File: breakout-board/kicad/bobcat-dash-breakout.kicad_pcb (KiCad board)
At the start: 2 copper layers, 162 x 159 mm, 184 parts, among them J1 TO PI (40-pin ribbon), J10 ADS1115 PWR/I2C, J11 LIGHTS, J12 COIL, J13 TILT, J14 TEMP PROBE, J15 ADS1115 INPUTS, J16 MAX98357A STEREO, J17 POD, J2 POWER IN, J3 TO 5V BUCK, J4 SWITCHES, J5 TACH, J6 FUEL, J7 HORN, J8 SILENCE, J9 MAX98357A MONO, Q1 IRLZ44N, Q2 IRF4905, Q3 BC547B, Q4 BC547B, Q5 IRLZ44N, U1 PC817, U10 PC817, U11 DS18B20, U4 PC817, U5 PC817, U6 CD4060BE, U7 PC817, U8 PC817, U9 PC817

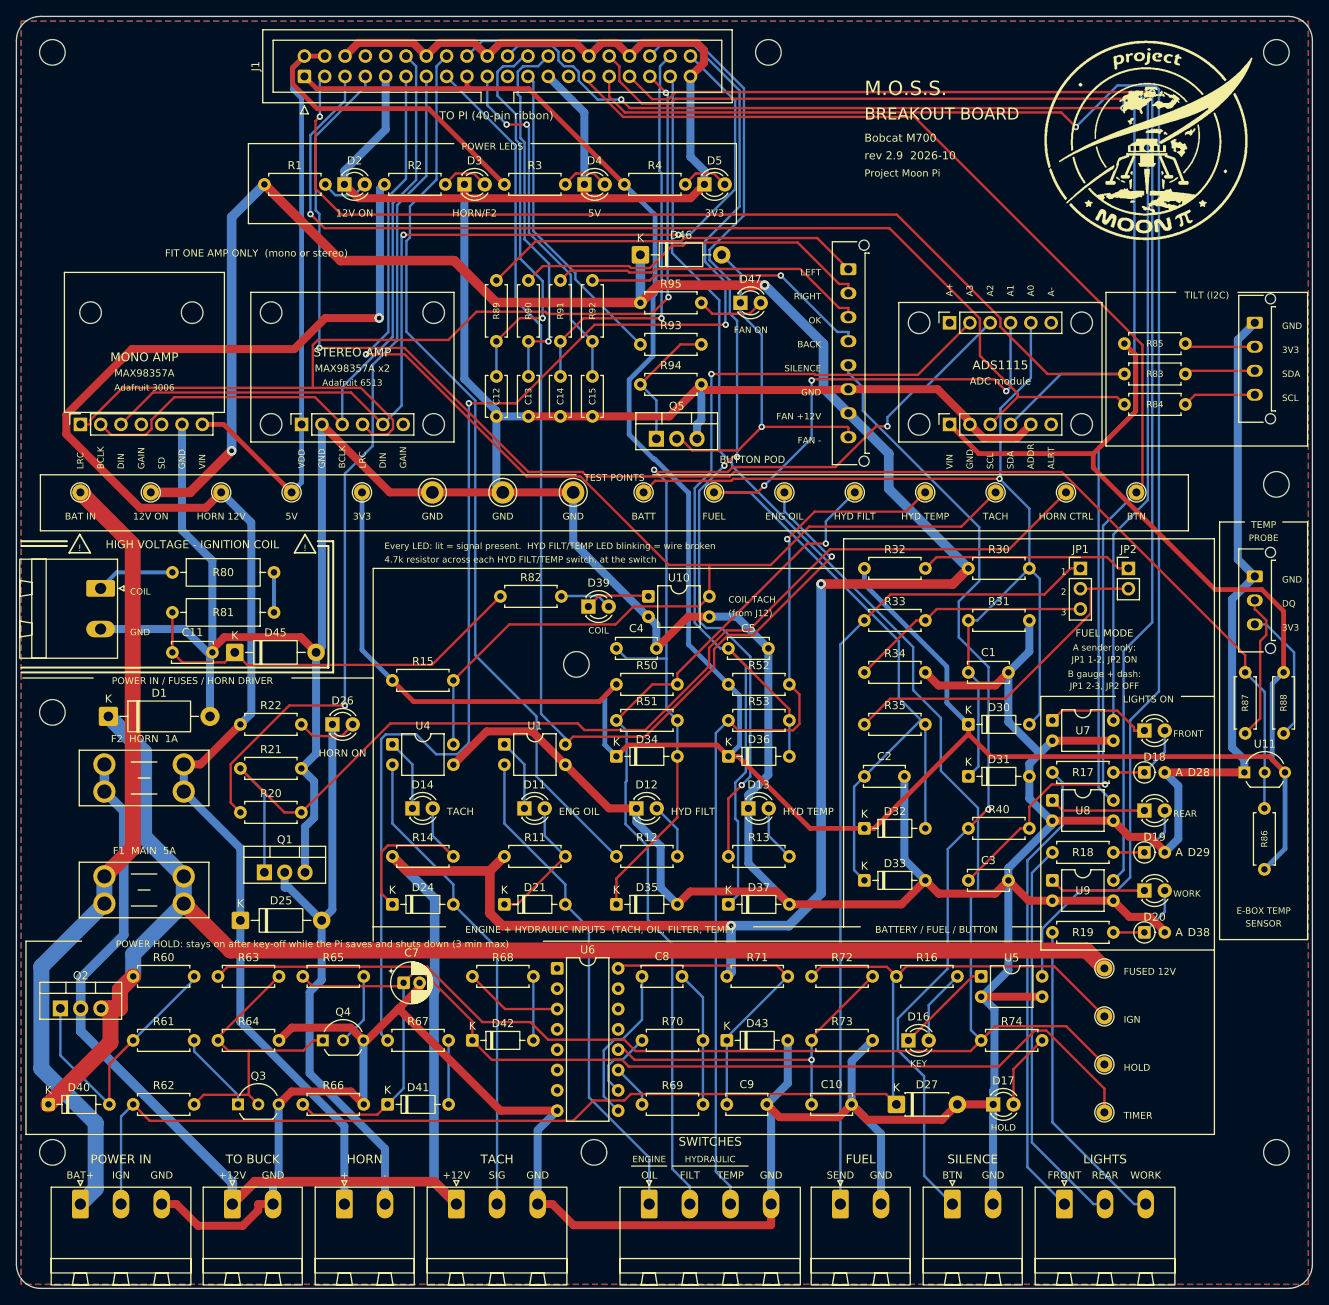
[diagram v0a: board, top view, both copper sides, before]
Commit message: Logo on the dash and web, SYSTEM > ABOUT, board rev 2.9 final (bigger logo, fun back)
Dash:
- Project Moon Pi patch in the header (splash/logo-small.png)
- SYSTEM > ABOUT: patch, system name, software version, board rev,
  computer model, engine hours, Wi-Fi name, source and font credit

Web:
- Patch in every page header (/logo/...), embedded in exported reports
- Software page opens with an About section

Board rev 2.9:
- Logo 30 mm (was 26) and further left, title block beside it
- Back silkscreen: fun lines and the dash's skid steer climbing a hill
- Routed, DRC and schematic parity clean; gerbers, BOM, renders updated

Tools: tools/make_logo.py makes the transparent logo pictures

Co-Authored-By: Claude Opus 5.5 <noreply@anthropic.com>
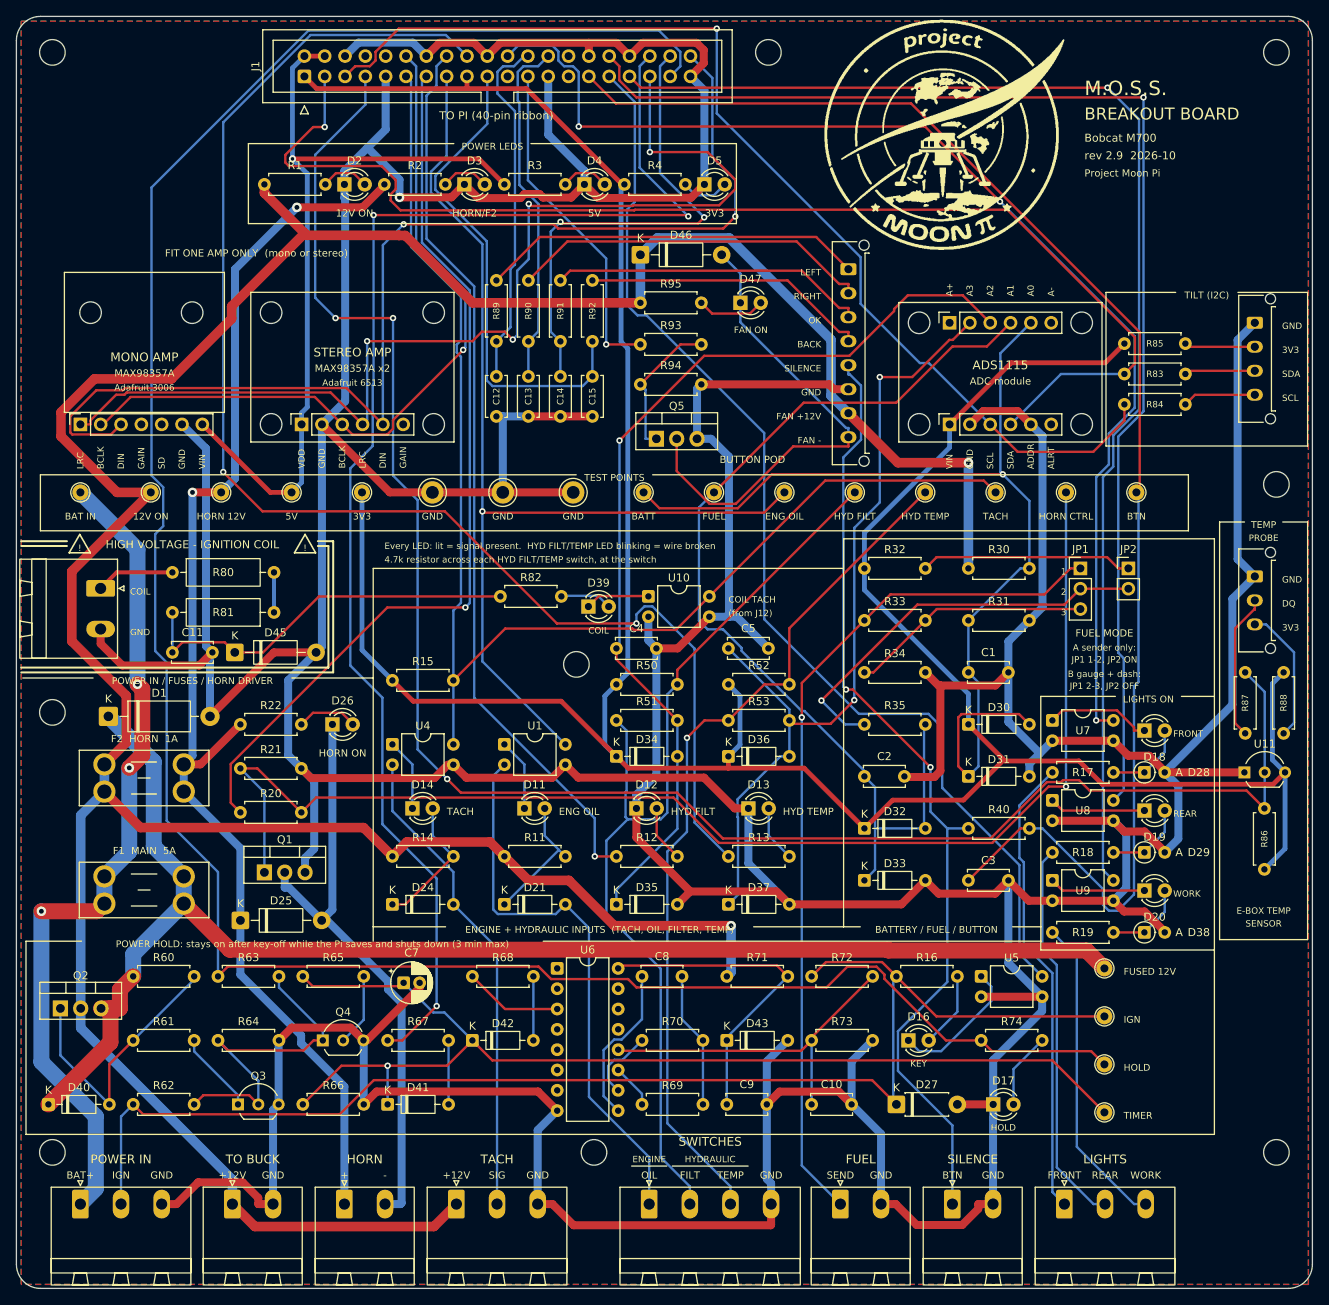
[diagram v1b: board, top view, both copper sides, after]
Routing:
- net KEY_GPIO: track 194.8 -> 141.5 mm, vias 1 -> 0
- net HOLD_GPIO: track 256.3 -> 300.7 mm
- net GND: track 1058.4 -> 1102.4 mm, vias 0 -> 1
- net W1_DQ: track 189.0 -> 229.2 mm, vias 1 -> 3
- net TEMP_LED: track 144.2 -> 178.0 mm, vias 3 -> 2
- net +3V3: track 418.2 -> 388.9 mm
- net +12V_HORN: track 191.0 -> 162.2 mm, vias 1 -> 2
- net HORN_G: track 138.3 -> 162.5 mm, vias 0 -> 1
- net +12V: track 441.0 -> 418.1 mm, vias 4 -> 2
- net TEMP_ADC: track 123.3 -> 104.3 mm, vias 1 -> 2
- net I2S_DIN: track 123.6 -> 142.2 mm
- net BTN_GPIO: track 164.3 -> 182.6 mm, vias 1 -> 0
- net BTN_BACK_GPIO: track 44.4 -> 61.7 mm, vias 2 -> 0
- net LT_FRONT_GPIO: track 166.0 -> 150.8 mm, vias 2 -> 3
- net OIL_GPIO: track 144.6 -> 130.1 mm
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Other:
- board text added: "DON'T LET THE MAGIC SMOKE OUT"
- board text added: "Houston, we have a breakout board"
- board text added: "Keep the shiny side up"
- board text added: "No bobcats were harmed in the making of this board"
- board text added: "One small step for man, one giant leap for skid-steer kind"
- board text added: "do you lift, bro?"
- board text added: "hi mom"

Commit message: Rev 3.0: cylinder head temps (CHT) and parking brake; new CHT + Parking Brake board
Software:
- cht.py: MCP9601 thermocouple amplifiers on I2C, per-cylinder limits
  (500 F warn, 550 F alarm + horn; factory head switches trip over 570 F),
  spread check vs the other cylinders' average, NO SIGNAL per cylinder.
  M.O.S.S. warns only, never stops the engine
- brake.py: (P) BRAKE tell-tale, PARKING BRAKE ON when working above idle
  with it set, SET PARKING BRAKE reminder at key-off
- Dash CYL HEAD TEMP tile, web Status tiles, Engine Status, alarm history,
  per-cylinder daily highs/lows in Reports; simulator keys ` and /
- [cht] and [park_brake] in config.toml (off until the hardware is fitted)

Breakout board rev 3.0:
- J18 AUX (Micro-Fit 2x3) to the CHT board: shared protected I2C,
  brake signal on GPIO 9 (R96 1k), brake LED feed from +12V (R97 2.2k)
- Routed, DRC and schematic parity clean; gerbers, BOM, renders, template

New breakout-board/cht-board (rev 1.0, 87 x 46 mm):
- Four sockets for Adafruit MCP9601 modules (address set by socket:
  0x60 / 0x65 / 0x66 / 0x67), parking brake optocoupler input, AUX plug
- Generator, KiCad project, gerbers, BOM, renders, README

BOM spreadsheet: CHT sensor, modules, Type K wire and connectors, brake switch

Co-Authored-By: Claude Opus 5.5 <noreply@anthropic.com>
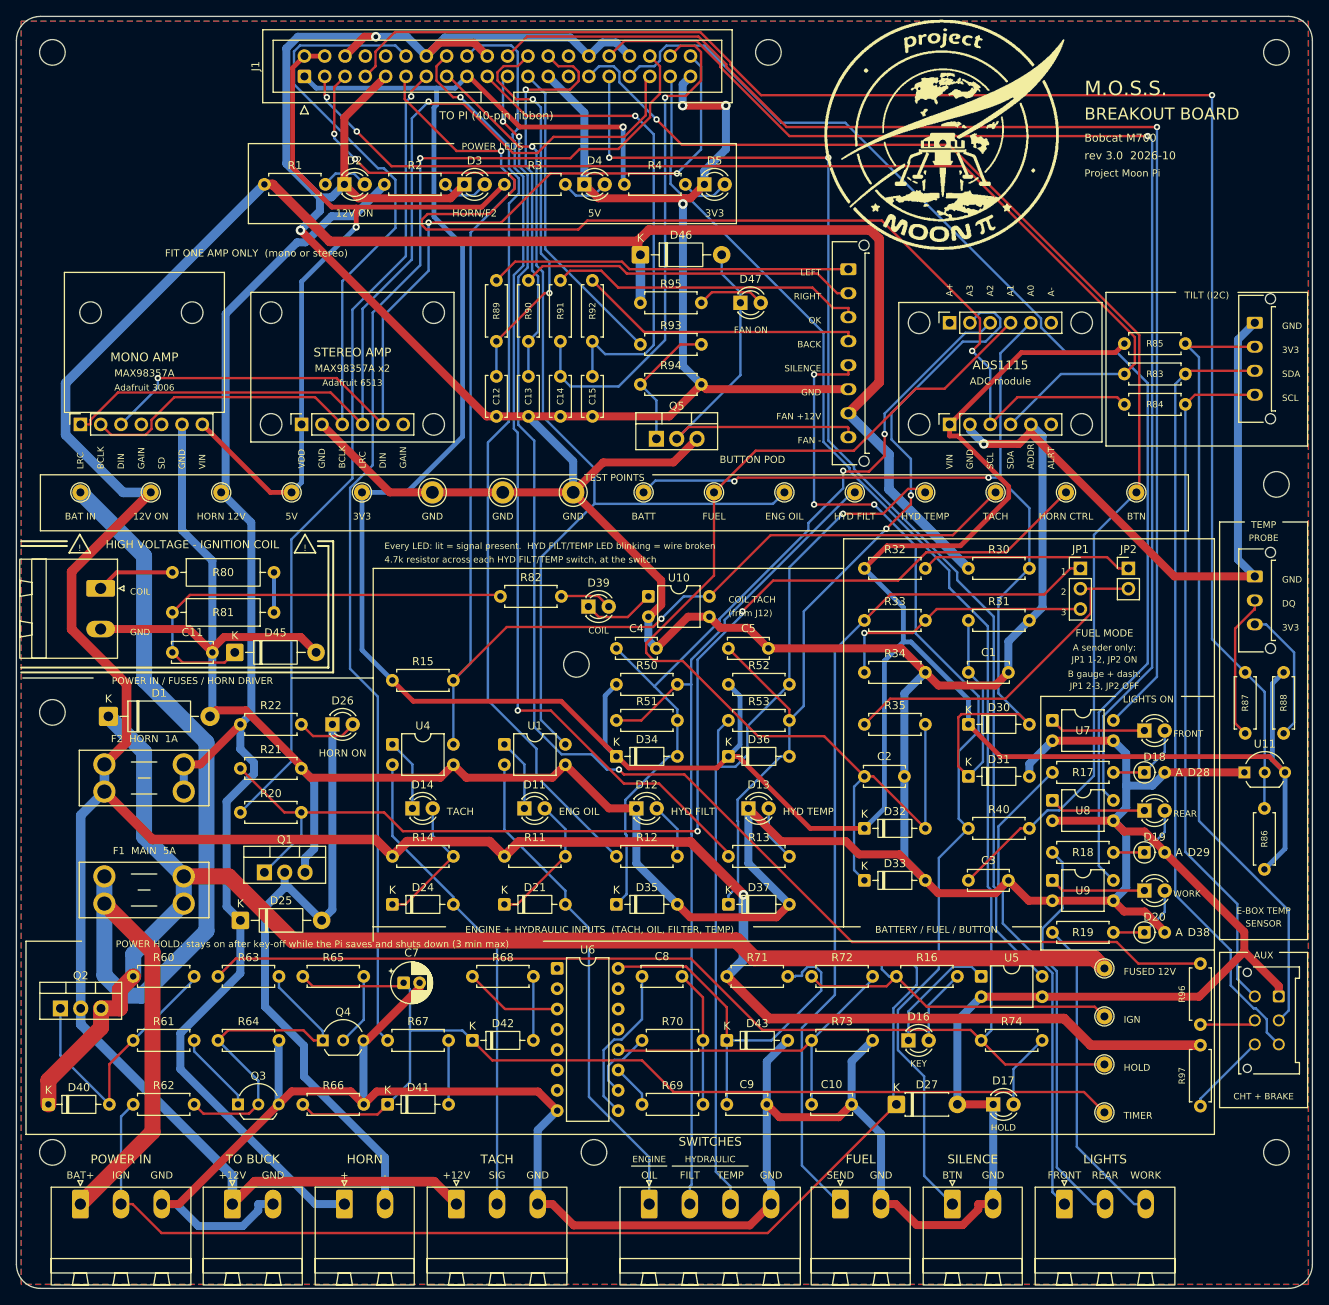
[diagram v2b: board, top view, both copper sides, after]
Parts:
- added J18: AUX (CHT + BRAKE), Connector_Molex:Molex_Micro-Fit_3.0_43045-0612_2x03_P3.00mm_Vertical, F.Cu at (157.8, 122.5)
- added R96: 1k, Resistor_THT:R_Axial_DIN0207_L6.3mm_D2.5mm_P7.62mm_Horizontal, F.Cu at (148.0, 118.4)
- added R97: 2.2k, Resistor_THT:R_Axial_DIN0207_L6.3mm_D2.5mm_P7.62mm_Horizontal, F.Cu at (148.0, 128.6)
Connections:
- net /TILT_3V3 renamed TILT_3V3
- net /TILT_SCL renamed TILT_SCL
- net /TILT_SDA renamed TILT_SDA
- J1 pad 21: unconnected-(J1-Pin_21-Pad21) -> BRAKE_GPIO
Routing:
- net BRAKE_GPIO: track 0.00 -> 179.7 mm, vias 0 -> 3
- net TILT_3V3: track 8.85 -> 99.3 mm
- net TILT_SDA: track 8.85 -> 98.7 mm
- net GND: track 1102.4 -> 1183.9 mm, vias 1 -> 6
- net TILT_SCL: track 9.18 -> 86.8 mm
- net +12V: track 418.1 -> 491.4 mm, vias 2 -> 1
- net TEMP_LED: track 178.0 -> 125.2 mm, vias 2 -> 1
- net HOLD_GPIO: track 300.7 -> 255.2 mm
- net +12V_IN: track 105.1 -> 134.7 mm, vias 3 -> 0
- net I2S_DIN: track 142.2 -> 115.9 mm, vias 2 -> 3
- net W1_DQ: track 229.2 -> 204.5 mm, vias 3 -> 1
- net SCL: track 135.7 -> 156.6 mm, vias 1 -> 3
- net BTN_GPIO: track 182.6 -> 162.6 mm, vias 0 -> 1
- net KILL_GPIO: track 174.9 -> 155.4 mm, vias 3 -> 1
- net I2S_LRC: track 136.0 -> 119.5 mm, vias 4 -> 1
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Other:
- board text added: "AUX"
- board text added: "CHT + BRAKE"
- board text added: "rev 3.0 2026-10"
- board text removed: "rev 2.9 2026-10"
